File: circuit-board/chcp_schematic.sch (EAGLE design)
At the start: 16 parts, among them IC1 ATMEGA328-20P, IC2 24MAC402, J1 FTDI, J2 LCD1, J3 LCD2, Q1 16 MHz

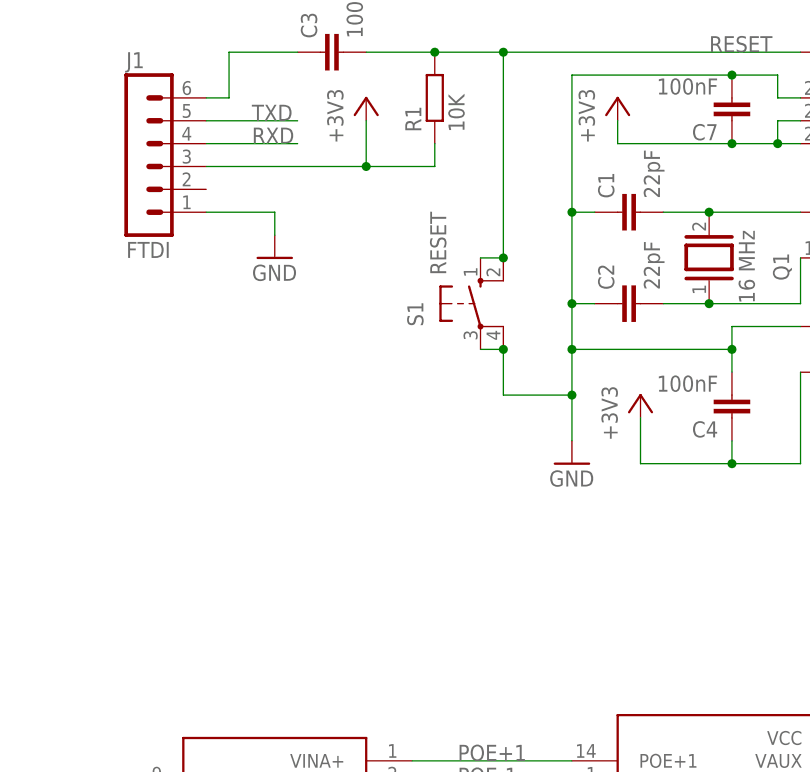
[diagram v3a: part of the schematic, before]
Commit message: Added 3mm Green Power LED
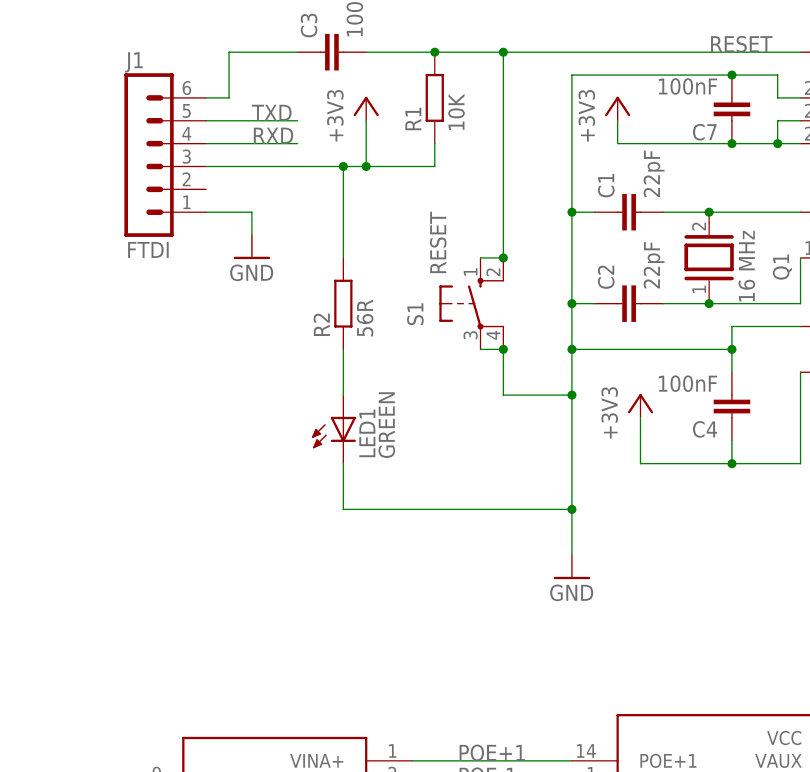
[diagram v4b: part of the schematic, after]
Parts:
- added LED1: GREEN, led:LED3MM
- added R2: 56R, rcl:R-EU_0204/7
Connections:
- new net N$8: LED1.A, R2.1
- net +3V3: now also R2.2
- net GND: now also LED1.C
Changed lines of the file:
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@@
 <part name="ETH1" library="in28j60" deviceset="IN28J60" device=""/>
 <part name="J3" library="con-lstb" deviceset="MA08-1" device="" value="LCD2"/>
+<part name="LED1" library="led" deviceset="LED" device="3MM" value="GREEN"/>
+<part name="R2" library="rcl" deviceset="R-EU_" device="0204/7" value="56R"/>
 </parts>
 <sheets>
@@
 <instance part="+3V1" gate="G$1" x="-43.18" y="22.86"/>
 <instance part="+3V2" gate="G$1" x="106.68" y="63.5"/>
-<instance part="GND1" gate="1" x="-50.8" y="15.24"/>
+<instance part="GND1" gate="1" x="-50.8" y="2.54"/>
 <instance part="GND2" gate="1" x="106.68" y="17.78"/>
 <instance part="GND4" gate="1" x="-109.22" y="-45.72"/>
 <instance part="+3V4" gate="G$1" x="-119.38" y="-15.24"/>
 <instance part="J1" gate="1" x="-99.06" y="50.8"/>
-<instance part="GND5" gate="1" x="-83.82" y="38.1"/>
+<instance part="GND5" gate="1" x="-86.36" y="38.1"/>
 <instance part="+3V5" gate="G$1" x="-73.66" y="55.88"/>
 <instance part="Q1" gate="G$1" x="-35.56" y="38.1" smashed="yes" rot="R90">
@@
 <instance part="ETH1" gate="G$1" x="-35.56" y="-27.94"/>
 <instance part="J3" gate="1" x="22.86" y="-30.48" rot="MR180"/>
+<instance part="LED1" gate="G$1" x="-76.2" y="20.32"/>
+<instance part="R2" gate="G$1" x="-76.2" y="33.02" rot="R90"/>
 </instances>
 <busses>
@@
 <pinref part="J1" gate="1" pin="3"/>
 <pinref part="+3V5" gate="G$1" pin="+3V3"/>
-<wire x1="-91.44" y1="48.26" x2="-73.66" y2="48.26" width="0.1524" layer="91"/>
+<wire x1="-91.44" y1="48.26" x2="-76.2" y2="48.26" width="0.1524" layer="91"/>
+<wire x1="-76.2" y1="48.26" x2="-73.66" y2="48.26" width="0.1524" layer="91"/>
 <wire x1="-73.66" y1="48.26" x2="-73.66" y2="53.34" width="0.1524" layer="91"/>
 <wire x1="-73.66" y1="48.26" x2="-66.04" y2="48.26" width="0.1524" layer="91"/>
@@
 <pinref part="R1" gate="G$1" pin="1"/>
 <wire x1="-66.04" y1="48.26" x2="-66.04" y2="50.8" width="0.1524" layer="91"/>
+<pinref part="R2" gate="G$1" pin="2"/>
+<wire x1="-76.2" y1="38.1" x2="-76.2" y2="48.26" width="0.1524" layer="91"/>
+<junction x="-76.2" y="48.26"/>
 </segment>
 <segment>
@@
 <segment>
 <pinref part="GND1" gate="1" pin="GND"/>
-<wire x1="-50.8" y1="17.78" x2="-50.8" y2="22.86" width="0.1524" layer="91"/>
+<wire x1="-50.8" y1="5.08" x2="-50.8" y2="10.16" width="0.1524" layer="91"/>
+<wire x1="-50.8" y1="10.16" x2="-50.8" y2="22.86" width="0.1524" layer="91"/>
 <wire x1="-50.8" y1="58.42" x2="-50.8" y2="43.18" width="0.1524" layer="91"/>
 <pinref part="C1" gate="G$1" pin="1"/>
@@
 <junction x="-33.02" y="27.94"/>
 <junction x="-50.8" y="27.94"/>
+<pinref part="LED1" gate="G$1" pin="C"/>
+<wire x1="-76.2" y1="15.24" x2="-76.2" y2="10.16" width="0.1524" layer="91"/>
+<wire x1="-76.2" y1="10.16" x2="-50.8" y2="10.16" width="0.1524" layer="91"/>
+<junction x="-50.8" y="10.16"/>
 </segment>
 <segment>
@@
 <segment>
 <pinref part="J1" gate="1" pin="1"/>
-<wire x1="-91.44" y1="43.18" x2="-83.82" y2="43.18" width="0.1524" layer="91"/>
+<wire x1="-91.44" y1="43.18" x2="-86.36" y2="43.18" width="0.1524" layer="91"/>
 <pinref part="GND5" gate="1" pin="GND"/>
-<wire x1="-83.82" y1="43.18" x2="-83.82" y2="40.64" width="0.1524" layer="91"/>
+<wire x1="-86.36" y1="43.18" x2="-86.36" y2="40.64" width="0.1524" layer="91"/>
 </segment>
 <segment>
@@
 </segment>
 </net>
+<net name="N$8" class="0">
+<segment>
+<pinref part="R2" gate="G$1" pin="1"/>
+<pinref part="LED1" gate="G$1" pin="A"/>
+<wire x1="-76.2" y1="27.94" x2="-76.2" y2="22.86" width="0.1524" layer="91"/>
+</segment>
+</net>

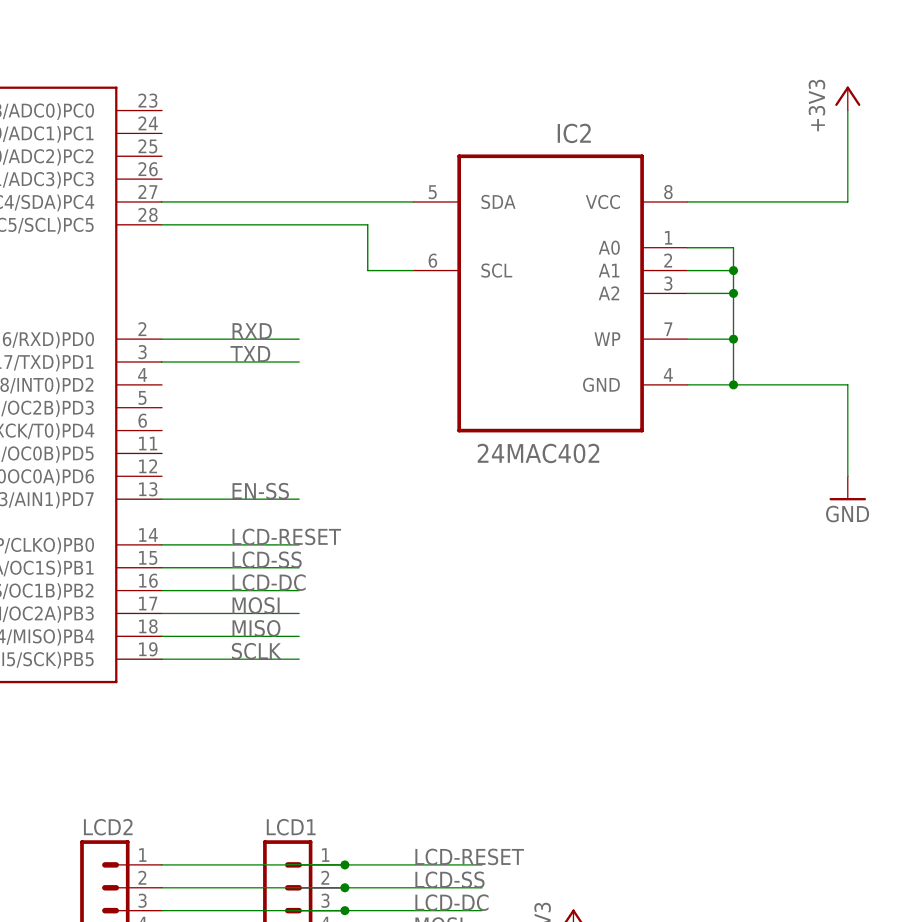
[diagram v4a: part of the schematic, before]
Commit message: Added Red LED and Push Button to the schematic
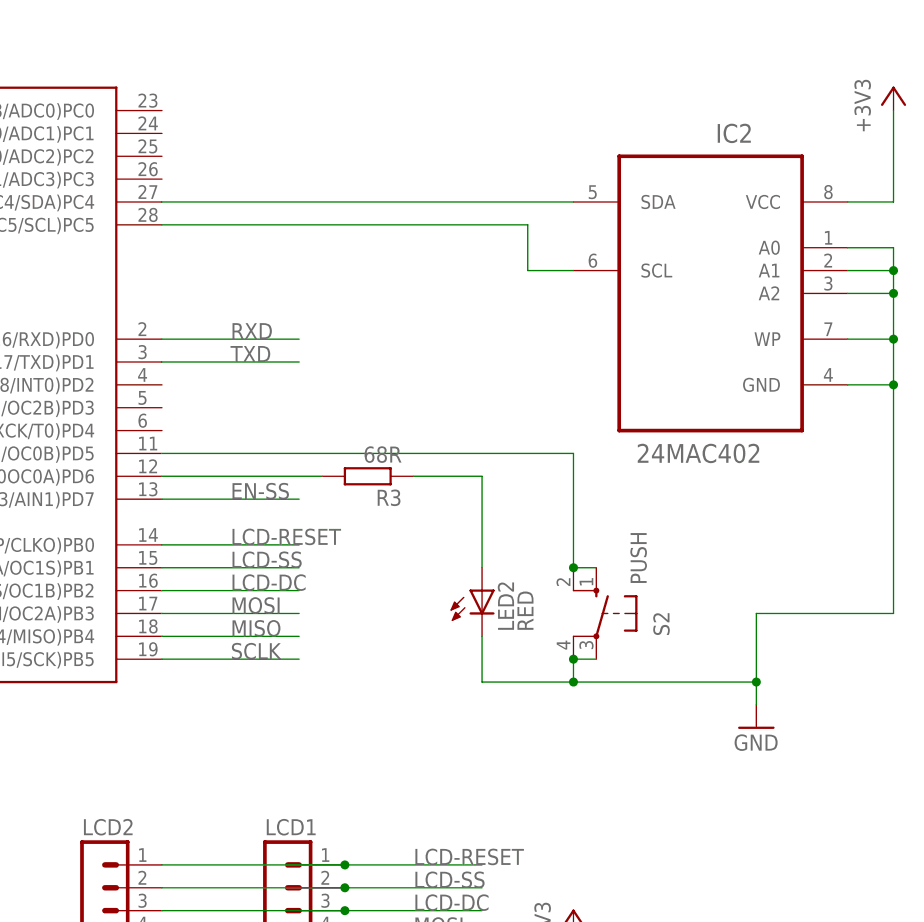
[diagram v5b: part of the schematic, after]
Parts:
- added LED2: RED, led:LED3MM
- added R3: 68R, rcl:R-EU_0204/7
- added S2: PUSH, switch-omron:10-XX
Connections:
- new net N$10: LED2.A, R3.1
- new net N$11: IC1.(PCI22/AIN0OC0A)PD6, R3.2
- new net N$13: IC1.(PCI21/T1/OC0B)PD5, S2.S, S2.S1
- net GND: now also LED2.C, S2.P, S2.P1
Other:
- moved on the sheet: IC2
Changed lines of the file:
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@@
 <?xml version="1.0" encoding="utf-8"?>
 <!DOCTYPE eagle SYSTEM "eagle.dtd">
-<eagle version="6.5.0">
+<eagle version="7.1.0">
 <drawing>
 <settings>
@@
 <part name="LED1" library="led" deviceset="LED" device="3MM" value="GREEN"/>
 <part name="R2" library="rcl" deviceset="R-EU_" device="0204/7" value="56R"/>
+<part name="LED2" library="led" deviceset="LED" device="3MM" value="RED"/>
+<part name="R3" library="rcl" deviceset="R-EU_" device="0204/7" value="68R"/>
+<part name="S2" library="switch-omron" deviceset="10-XX" device="" value="PUSH"/>
 </parts>
 <sheets>
@@
 <instances>
 <instance part="IC1" gate="G$1" x="-2.54" y="33.02"/>
-<instance part="IC2" gate="A" x="73.66" y="43.18" rot="MR0"/>
+<instance part="IC2" gate="A" x="91.44" y="43.18" rot="MR0"/>
 <instance part="+3V1" gate="G$1" x="-43.18" y="22.86"/>
-<instance part="+3V2" gate="G$1" x="106.68" y="63.5"/>
+<instance part="+3V2" gate="G$1" x="111.76" y="63.5"/>
 <instance part="GND1" gate="1" x="-50.8" y="2.54"/>
-<instance part="GND2" gate="1" x="106.68" y="17.78"/>
+<instance part="GND2" gate="1" x="96.52" y="-7.62"/>
 <instance part="GND4" gate="1" x="-109.22" y="-45.72"/>
 <instance part="+3V4" gate="G$1" x="-119.38" y="-15.24"/>
@@
 <instance part="LED1" gate="G$1" x="-76.2" y="20.32"/>
 <instance part="R2" gate="G$1" x="-76.2" y="33.02" rot="R90"/>
+<instance part="LED2" gate="G$1" x="66.04" y="7.62"/>
+<instance part="R3" gate="G$1" x="53.34" y="20.32" rot="R180"/>
+<instance part="S2" gate="1" x="78.74" y="5.08" rot="MR0"/>
 </instances>
 <busses>
@@
 <pinref part="IC2" gate="A" pin="VCC"/>
 <pinref part="+3V2" gate="G$1" pin="+3V3"/>
-<wire x1="88.9" y1="50.8" x2="106.68" y2="50.8" width="0.1524" layer="91"/>
-<wire x1="106.68" y1="50.8" x2="106.68" y2="60.96" width="0.1524" layer="91"/>
+<wire x1="106.68" y1="50.8" x2="111.76" y2="50.8" width="0.1524" layer="91"/>
+<wire x1="111.76" y1="50.8" x2="111.76" y2="60.96" width="0.1524" layer="91"/>
 </segment>
 <segment>
@@
 <segment>
 <pinref part="GND2" gate="1" pin="GND"/>
-<wire x1="106.68" y1="20.32" x2="106.68" y2="30.48" width="0.1524" layer="91"/>
+<wire x1="96.52" y1="-5.08" x2="96.52" y2="-2.54" width="0.1524" layer="91"/>
+<wire x1="96.52" y1="-2.54" x2="96.52" y2="5.08" width="0.1524" layer="91"/>
+<wire x1="96.52" y1="5.08" x2="111.76" y2="5.08" width="0.1524" layer="91"/>
 <pinref part="IC2" gate="A" pin="GND"/>
-<wire x1="106.68" y1="30.48" x2="93.98" y2="30.48" width="0.1524" layer="91"/>
 <pinref part="IC2" gate="A" pin="WP"/>
-<wire x1="93.98" y1="30.48" x2="88.9" y2="30.48" width="0.1524" layer="91"/>
-<wire x1="88.9" y1="35.56" x2="93.98" y2="35.56" width="0.1524" layer="91"/>
-<wire x1="93.98" y1="35.56" x2="93.98" y2="30.48" width="0.1524" layer="91"/>
-<junction x="93.98" y="30.48"/>
+<wire x1="111.76" y1="30.48" x2="106.68" y2="30.48" width="0.1524" layer="91"/>
+<wire x1="106.68" y1="35.56" x2="111.76" y2="35.56" width="0.1524" layer="91"/>
+<wire x1="111.76" y1="35.56" x2="111.76" y2="30.48" width="0.1524" layer="91"/>
 <pinref part="IC2" gate="A" pin="A2"/>
-<wire x1="88.9" y1="40.64" x2="93.98" y2="40.64" width="0.1524" layer="91"/>
-<wire x1="93.98" y1="40.64" x2="93.98" y2="35.56" width="0.1524" layer="91"/>
-<junction x="93.98" y="35.56"/>
+<wire x1="106.68" y1="40.64" x2="111.76" y2="40.64" width="0.1524" layer="91"/>
+<wire x1="111.76" y1="40.64" x2="111.76" y2="35.56" width="0.1524" layer="91"/>
+<junction x="111.76" y="35.56"/>
 <pinref part="IC2" gate="A" pin="A1"/>
-<wire x1="88.9" y1="43.18" x2="93.98" y2="43.18" width="0.1524" layer="91"/>
-<wire x1="93.98" y1="43.18" x2="93.98" y2="40.64" width="0.1524" layer="91"/>
-<junction x="93.98" y="40.64"/>
+<wire x1="106.68" y1="43.18" x2="111.76" y2="43.18" width="0.1524" layer="91"/>
+<wire x1="111.76" y1="43.18" x2="111.76" y2="40.64" width="0.1524" layer="91"/>
+<junction x="111.76" y="40.64"/>
 <pinref part="IC2" gate="A" pin="A0"/>
-<wire x1="88.9" y1="45.72" x2="93.98" y2="45.72" width="0.1524" layer="91"/>
-<wire x1="93.98" y1="45.72" x2="93.98" y2="43.18" width="0.1524" layer="91"/>
-<junction x="93.98" y="43.18"/>
+<wire x1="106.68" y1="45.72" x2="111.76" y2="45.72" width="0.1524" layer="91"/>
+<wire x1="111.76" y1="45.72" x2="111.76" y2="43.18" width="0.1524" layer="91"/>
+<junction x="111.76" y="43.18"/>
+<wire x1="111.76" y1="5.08" x2="111.76" y2="30.48" width="0.1524" layer="91"/>
+<junction x="111.76" y="30.48"/>
+<pinref part="S2" gate="1" pin="P1"/>
+<pinref part="S2" gate="1" pin="P"/>
+<wire x1="78.74" y1="0" x2="76.2" y2="0" width="0.1524" layer="91"/>
+<wire x1="76.2" y1="0" x2="76.2" y2="-2.54" width="0.1524" layer="91"/>
+<junction x="76.2" y="0"/>
+<wire x1="76.2" y1="-2.54" x2="96.52" y2="-2.54" width="0.1524" layer="91"/>
+<junction x="96.52" y="-2.54"/>
+<pinref part="LED2" gate="G$1" pin="C"/>
+<wire x1="66.04" y1="2.54" x2="66.04" y2="-2.54" width="0.1524" layer="91"/>
+<wire x1="66.04" y1="-2.54" x2="76.2" y2="-2.54" width="0.1524" layer="91"/>
+<junction x="76.2" y="-2.54"/>
 </segment>
 <segment>
@@
 <pinref part="IC2" gate="A" pin="SDA"/>
 <pinref part="IC1" gate="G$1" pin="(PCI12/ADC4/SDA)PC4"/>
-<wire x1="58.42" y1="50.8" x2="30.48" y2="50.8" width="0.1524" layer="91"/>
+<wire x1="76.2" y1="50.8" x2="30.48" y2="50.8" width="0.1524" layer="91"/>
 </segment>
 </net>
@@
 <segment>
 <pinref part="IC2" gate="A" pin="SCL"/>
-<wire x1="58.42" y1="43.18" x2="53.34" y2="43.18" width="0.1524" layer="91"/>
-<wire x1="53.34" y1="43.18" x2="53.34" y2="48.26" width="0.1524" layer="91"/>
+<wire x1="76.2" y1="43.18" x2="71.12" y2="43.18" width="0.1524" layer="91"/>
+<wire x1="71.12" y1="43.18" x2="71.12" y2="48.26" width="0.1524" layer="91"/>
 <pinref part="IC1" gate="G$1" pin="(PCI13/ADC5/SCL)PC5"/>
-<wire x1="53.34" y1="48.26" x2="30.48" y2="48.26" width="0.1524" layer="91"/>
+<wire x1="71.12" y1="48.26" x2="30.48" y2="48.26" width="0.1524" layer="91"/>
 </segment>
 </net>
@@
 </segment>
 </net>
+<net name="N$10" class="0">
+<segment>
+<pinref part="LED2" gate="G$1" pin="A"/>
+<wire x1="66.04" y1="20.32" x2="66.04" y2="10.16" width="0.1524" layer="91"/>
+<pinref part="R3" gate="G$1" pin="1"/>
+<wire x1="66.04" y1="20.32" x2="58.42" y2="20.32" width="0.1524" layer="91"/>
+</segment>
+</net>
+<net name="N$13" class="0">
+<segment>
+<pinref part="S2" gate="1" pin="S1"/>
+<pinref part="S2" gate="1" pin="S"/>
+<wire x1="78.74" y1="10.16" x2="76.2" y2="10.16" width="0.1524" layer="91"/>
+<pinref part="IC1" gate="G$1" pin="(PCI21/T1/OC0B)PD5"/>
+<wire x1="30.48" y1="22.86" x2="76.2" y2="22.86" width="0.1524" layer="91"/>
+<wire x1="76.2" y1="22.86" x2="76.2" y2="10.16" width="0.1524" layer="91"/>
+<junction x="76.2" y="10.16"/>
+</segment>
+</net>
+<net name="N$11" class="0">
+<segment>
+<pinref part="R3" gate="G$1" pin="2"/>
+<pinref part="IC1" gate="G$1" pin="(PCI22/AIN0OC0A)PD6"/>
+<wire x1="48.26" y1="20.32" x2="30.48" y2="20.32" width="0.1524" layer="91"/>
+</segment>
+</net>
